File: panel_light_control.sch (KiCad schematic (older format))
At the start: 70 parts, among them J1 Conn_01x02, J6 Conn_01x04, Q1 IRF540N, Q2 IRF540N, Q3 IRF540N, U1 L7805, U2 LM324

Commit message: RGB current sink placed and routed. All placement should be done now, next: check barrel jack footprint, do power routing, think about input protection for GPIOs, possibly add resistor arrays, route GP signals.
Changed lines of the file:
@@
 	8950 1850 9150 1850
-Wire Wire Line
-	7450 2150 7150 2150
-Connection ~ 7150 2150
-Wire Wire Line
-	7150 2150 7150 2300
-Wire Wire Line
-	6700 2150 6800 2150
-Wire Wire Line
-	6800 2300 6800 2150
-Connection ~ 6800 2150
-Wire Wire Line
-	6800 2150 7150 2150
 Wire Wire Line
 	6800 2600 6800 2700
@@
 	0    -1   1    0
 $EndComp
+Wire Wire Line
+	6800 2150 6700 2150
+Wire Wire Line
+	6800 2150 6800 2300
+Wire Wire Line
+	6800 2150 7150 2150
+Wire Wire Line
+	7150 2150 7150 2300
+Connection ~ 6800 2150
+Wire Wire Line
+	7150 2150 7450 2150
+Connection ~ 7150 2150
 $EndSCHEMATC

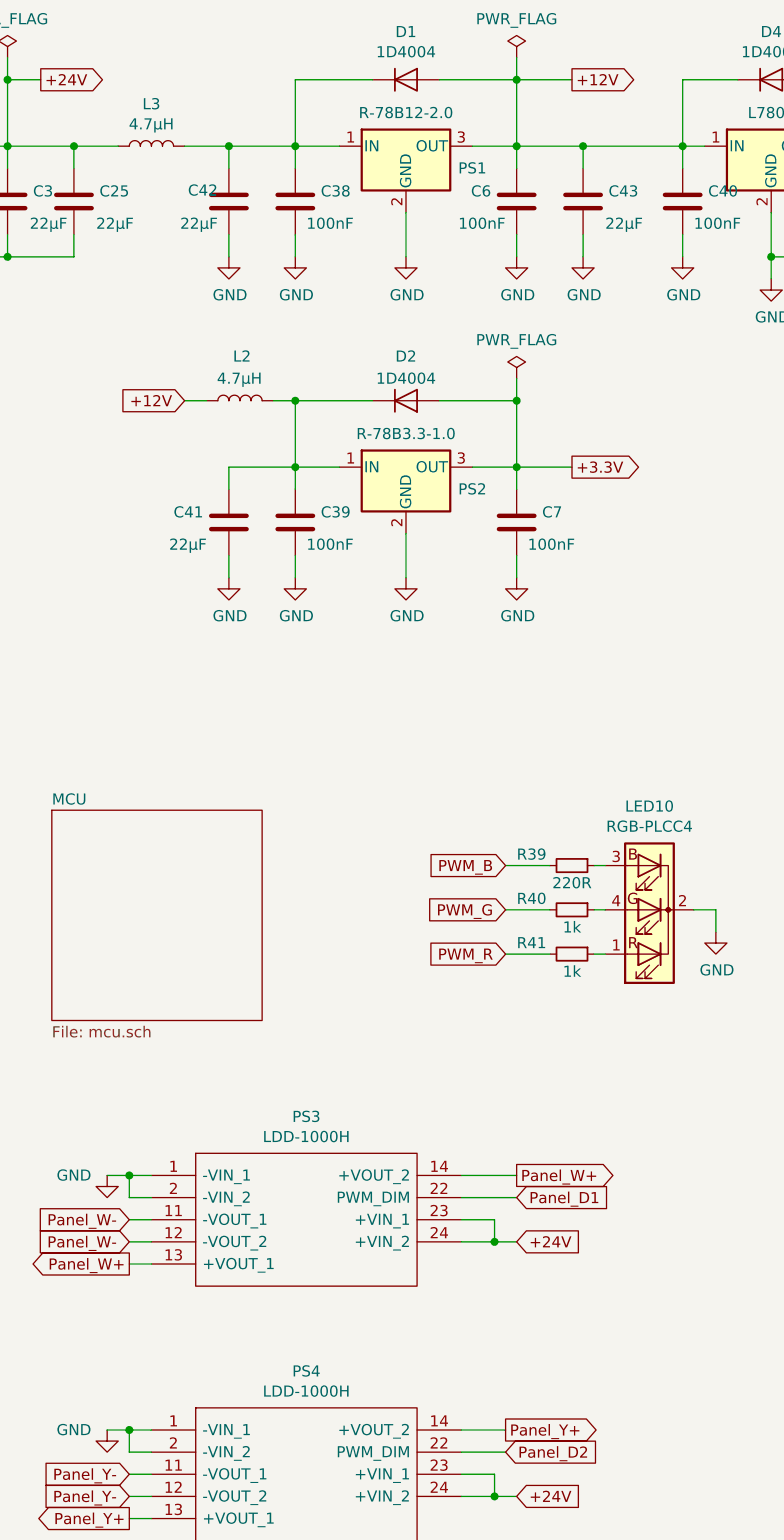
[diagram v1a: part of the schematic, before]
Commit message: PS1-> Panel1, PS2-> Panel2, PS12->12V, PS33-> 3.3V.
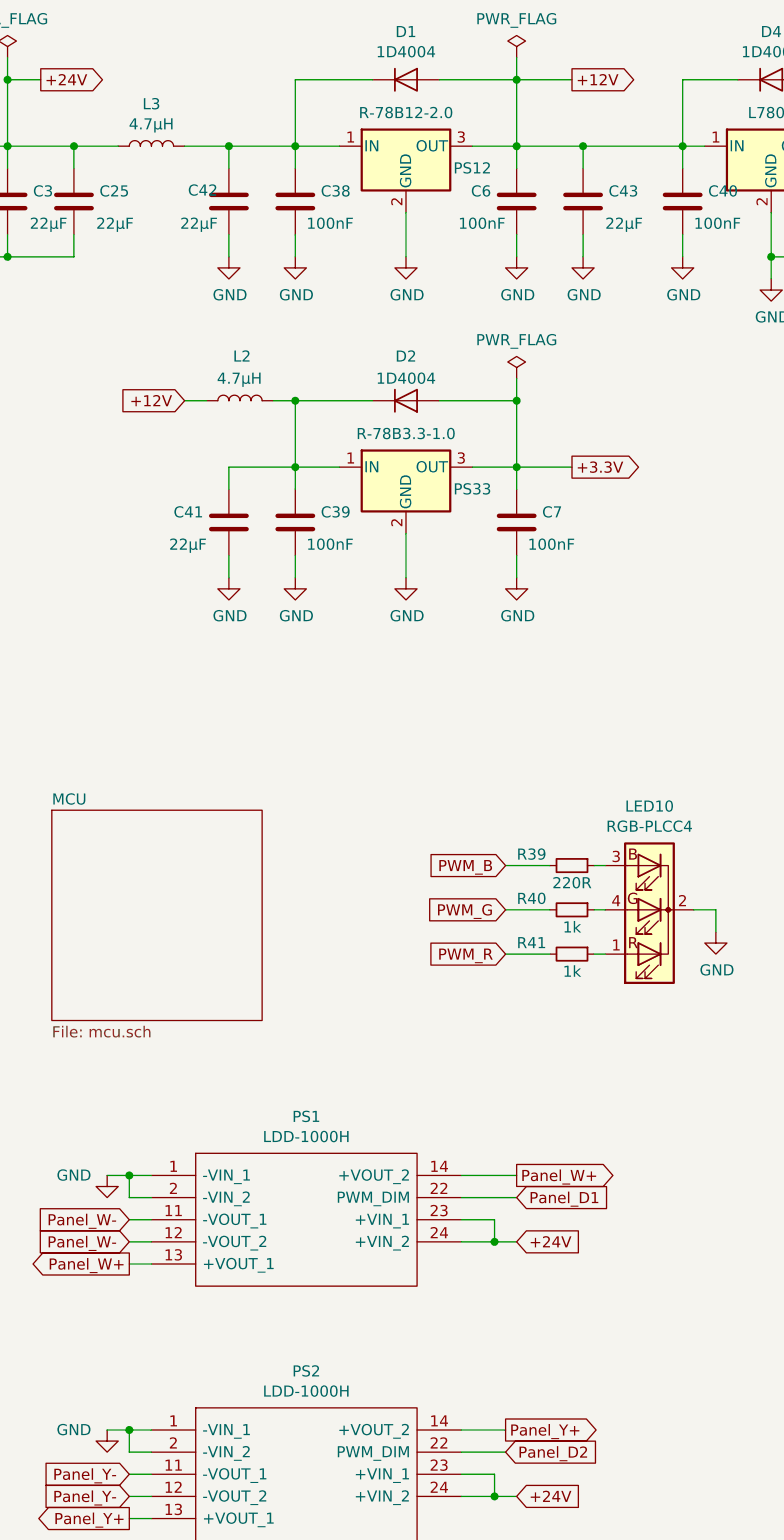
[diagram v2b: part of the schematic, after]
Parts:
- renumbered PS3 to PS1, PS1 to PS12, PS4 to PS2, PS2 to PS33
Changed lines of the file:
@@
 Connection ~ 2000 1200
 $Comp
-L panel_light_control-rescue:LDD-1000H-SamacSys_Parts PS4
+L panel_light_control-rescue:LDD-1000H-SamacSys_Parts PS2
 U 1 1 5BB7E2A0
 P 2650 7000
-F 0 "PS4" H 3350 7265 50  0000 C CNN
+F 0 "PS2" H 3350 7265 50  0000 C CNN
 F 1 "LDD-1000H" H 3350 7174 50  0000 C CNN
 F 2 "SamacSys_Parts:LDD-700H" H 3900 7100 50  0001 L CNN
@@
 $EndComp
 $Comp
-L panel_light_control-rescue:LDD-1000H-SamacSys_Parts PS3
+L panel_light_control-rescue:LDD-1000H-SamacSys_Parts PS1
 U 1 1 5BB8F859
 P 2650 5850
-F 0 "PS3" H 3350 6115 50  0000 C CNN
+F 0 "PS1" H 3350 6115 50  0000 C CNN
 F 1 "LDD-1000H" H 3350 6024 50  0000 C CNN
 F 2 "SamacSys_Parts:LDD-700H" H 3900 5950 50  0001 L CNN
@@
 $EndComp
 $Comp
-L Regulator_Switching:R-78B12-2.0 PS1
+L Regulator_Switching:R-78B12-2.0 PS12
 U 1 1 5BB902DF
 P 3800 1200
-F 0 "PS1" H 4100 1100 50  0000 C CNN
+F 0 "PS12" H 4100 1100 50  0000 C CNN
 F 1 "R-78B12-2.0" H 3800 1350 50  0000 C CNN
 F 2 "Converter_DCDC:Converter_DCDC_RECOM_R-78B-2.0_THT" H 4750 1300 50  0001 L CNN
@@
 $EndComp
 $Comp
-L Regulator_Switching:R-78B3.3-2.0 PS2
+L Regulator_Switching:R-78B3.3-2.0 PS33
 U 1 1 5BB90449
 P 3800 2650
-F 0 "PS2" H 4100 2550 50  0000 C CNN
+F 0 "PS33" H 4100 2550 50  0000 C CNN
 F 1 "R-78B3.3-1.0" H 3800 2800 50  0000 C CNN
 F 2 "Converter_DCDC:Converter_DCDC_RECOM_R-78B-2.0_THT" H 4850 2750 50  0001 L CNN

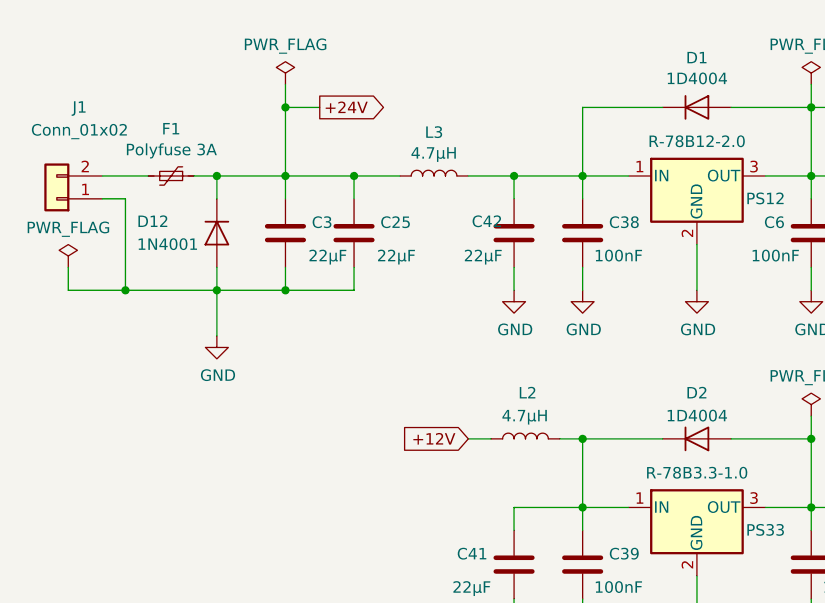
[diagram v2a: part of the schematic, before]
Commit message: add CAN termination jumper, switch-mode DCDC power routing and current sink routing done. Barrel jacks still need swapping?
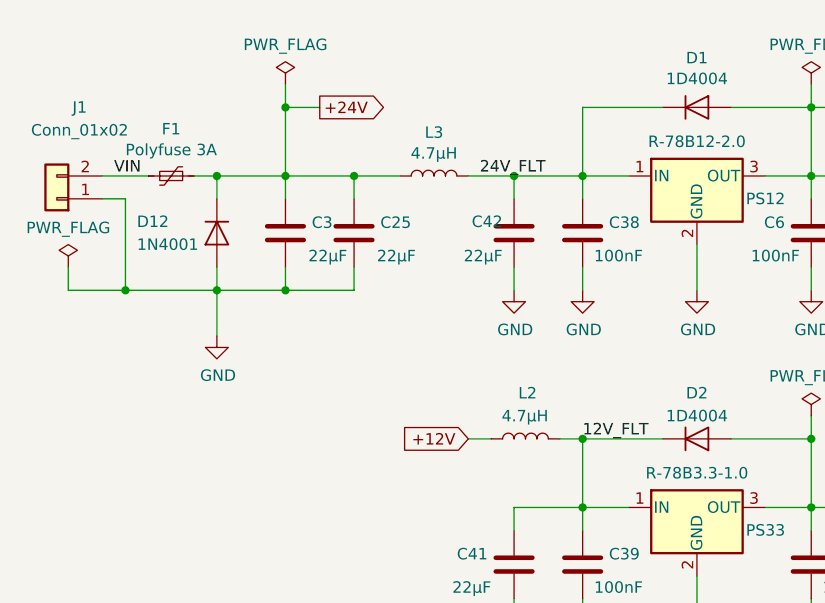
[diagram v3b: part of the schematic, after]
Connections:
- net VIN: now reaches F1.2, J1.2 (Pin_2)
- net 24V_FLT: now reaches C38.1, C42.1, D1.1 (K), L3.2, PS12.1 (IN)
- net 12V_FLT: now reaches C39.1, C41.1, D2.1 (K), L2.2, PS33.1 (IN)
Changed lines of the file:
@@
 	7150 2150 7450 2150
 Connection ~ 7150 2150
+Text Label 1250 1200 0    50   ~ 0
+VIN
+Text Label 2850 1200 0    50   ~ 0
+24V_FLT
+Text Label 3300 2350 0    50   ~ 0
+12V_FLT
 $EndSCHEMATC

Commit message: change I2S connector footprint back from 11 pin to 10 pin (MCK, SCK, WS... missing something?). More silkscreen clean-up and a bit of routing.
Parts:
- JTAG1: value Conn_01x06 -> Conn_01x07; footprint Connector_JST:JST_PH_S6B-PH-K_1x06_P2.00mm_Horizontal -> Connector_JST:JST_PH_S7B-PH-K_1x07_P2.00mm_Horizontal; symbol Connector_Generic:Conn_01x06 -> Connector_Generic:Conn_01x07
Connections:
- net +3.3V: now also JTAG1.7 (Pin_7)
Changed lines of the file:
@@
 	10400 5300 10200 5300
 $Comp
-L Connector_Generic:Conn_01x06 JTAG1
+L Connector_Generic:Conn_01x07 JTAG1
 U 1 1 5C66DBBA
-P 10600 2100
-F 0 "JTAG1" H 10680 2092 50  0000 L CNN
-F 1 "Conn_01x06" H 10680 2001 50  0000 L CNN
-F 2 "Connector_JST:JST_PH_S6B-PH-K_1x06_P2.00mm_Horizontal" H 10600 2100 50  0001 C CNN
-F 3 "~" H 10600 2100 50  0001 C CNN
-	1    10600 2100
-	1    0    0    -1
-$EndComp
-Text GLabel 10200 1900 0    50   Input ~ 0
+P 10600 2050
+F 0 "JTAG1" H 10680 2042 50  0000 L CNN
+F 1 "Conn_01x07" H 10680 1951 50  0000 L CNN
+F 2 "Connector_JST:JST_PH_S7B-PH-K_1x07_P2.00mm_Horizontal" H 10600 2050 50  0001 C CNN
+F 3 "~" H 10600 2050 50  0001 C CNN
+	1    10600 2050
+	1    0    0    -1
+$EndComp
+Text GLabel 10200 1750 0    50   Input ~ 0
 JTMS
-Text GLabel 10200 2000 0    50   Input ~ 0
+Text GLabel 10200 1850 0    50   Input ~ 0
 JTCK
-Text GLabel 10200 2100 0    50   Input ~ 0
+Text GLabel 10200 1950 0    50   Input ~ 0
 JTDI
-Text GLabel 10200 2200 0    50   Input ~ 0
+Text GLabel 10200 2050 0    50   Input ~ 0
 JTDO
-Text GLabel 10200 2300 0    50   Input ~ 0
+Text GLabel 10200 2150 0    50   Input ~ 0
 JTRST
 Wire Wire Line
-	10400 1900 10200 1900
-Wire Wire Line
-	10200 2000 10400 2000
-Wire Wire Line
-	10400 2100 10200 2100
-Wire Wire Line
-	10200 2200 10400 2200
-Wire Wire Line
-	10400 2300 10200 2300
+	10400 1750 10200 1750
+Wire Wire Line
+	10200 1850 10400 1850
+Wire Wire Line
+	10400 1950 10200 1950
+Wire Wire Line
+	10200 2050 10400 2050
+Wire Wire Line
+	10400 2150 10200 2150
 $Comp
 L power:GND #PWR04
 U 1 1 5C8842DC
-P 10300 2400
-F 0 "#PWR04" H 10300 2150 50  0001 C CNN
-F 1 "GND" H 10150 2350 50  0000 C CNN
-F 2 "" H 10300 2400 50  0001 C CNN
-F 3 "" H 10300 2400 50  0001 C CNN
-	1    10300 2400
-	1    0    0    -1
-$EndComp
-Wire Wire Line
-	10300 2400 10400 2400
+P 10300 2450
+F 0 "#PWR04" H 10300 2200 50  0001 C CNN
+F 1 "GND" H 10150 2400 50  0000 C CNN
+F 2 "" H 10300 2450 50  0001 C CNN
+F 3 "" H 10300 2450 50  0001 C CNN
+	1    10300 2450
+	1    0    0    -1
+$EndComp
+Wire Wire Line
+	10300 2250 10400 2250
 Text GLabel 10200 4800 0    50   Input ~ 0
 SPI0_CS0
@@
 Text Label 3300 2350 0    50   ~ 0
 12V_FLT
+Text GLabel 10200 2350 0    50   Input ~ 0
++3.3V
+Wire Wire Line
+	10200 2350 10400 2350
+Wire Wire Line
+	10300 2250 10300 2450
 $EndSCHEMATC

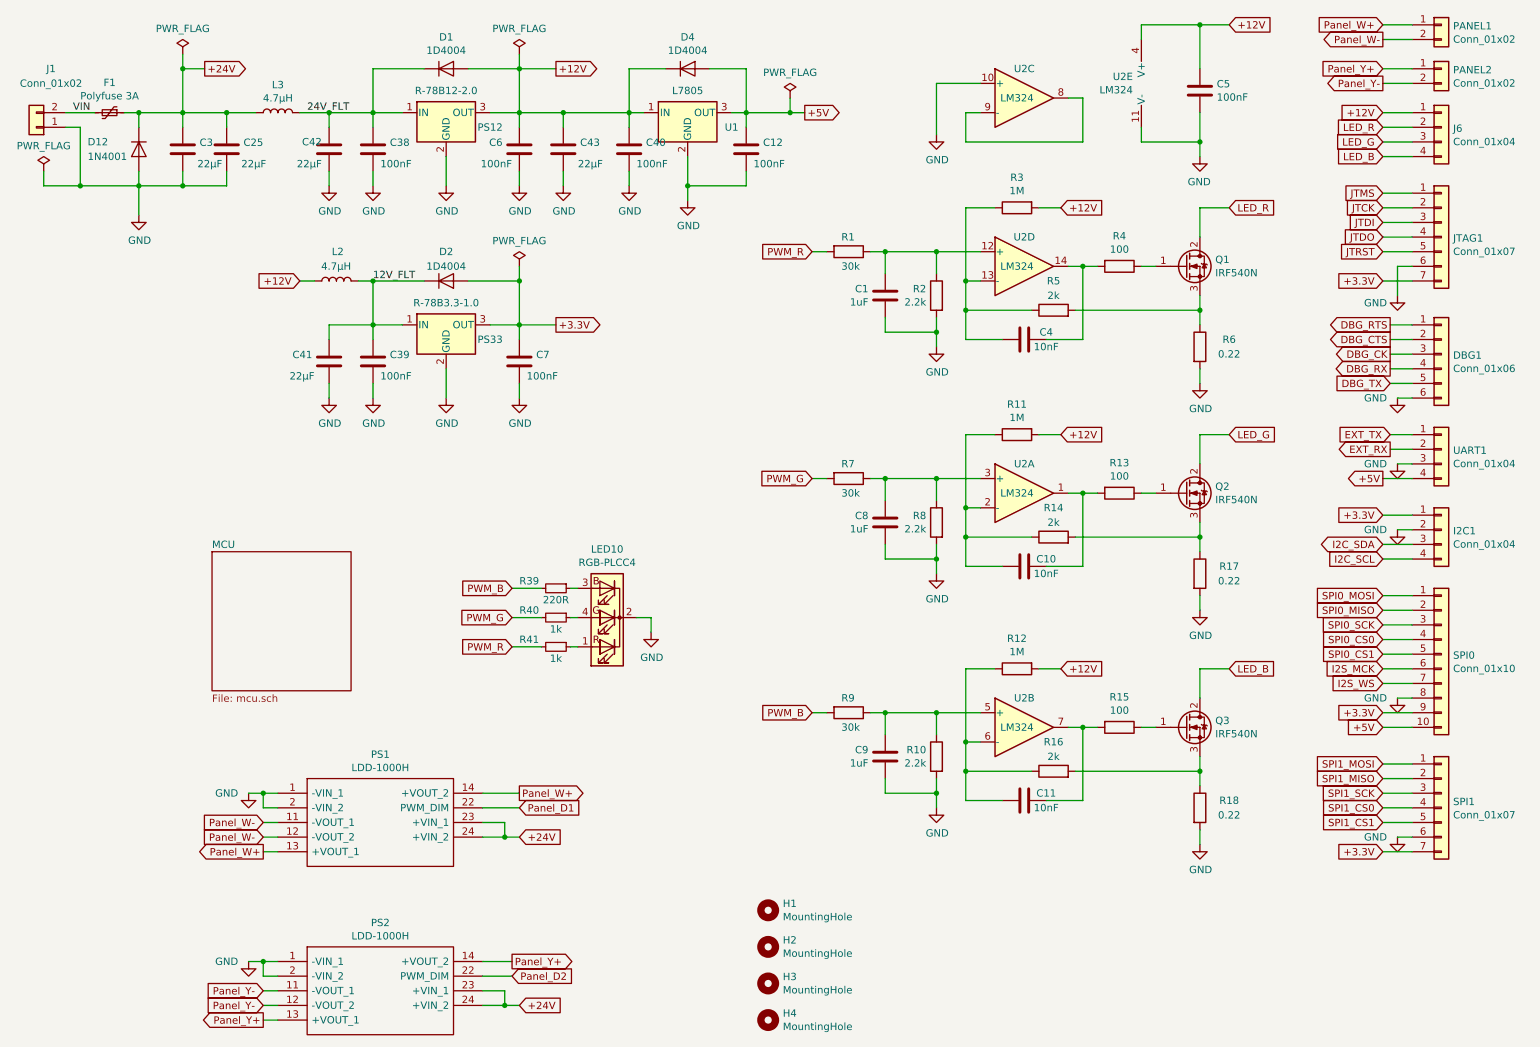
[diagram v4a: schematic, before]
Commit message: routing almost done. ToDo: fix symbols to include shielding on some connectors. finish routing. Add GND copper pour on bottom side.
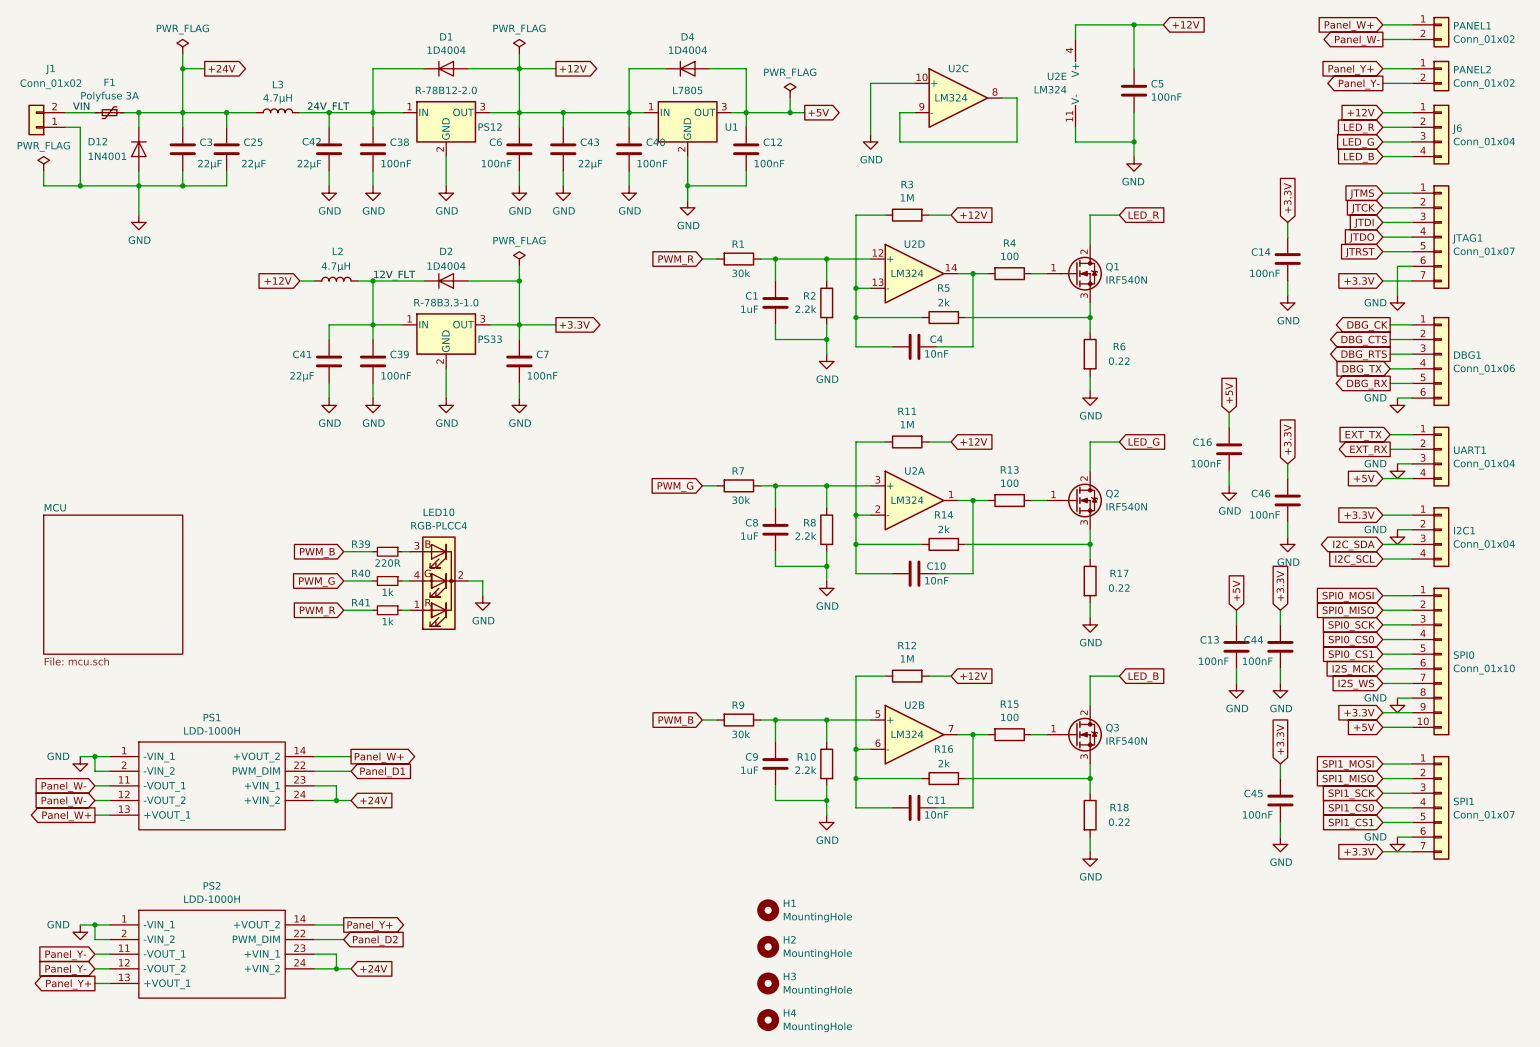
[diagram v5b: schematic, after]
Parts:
- added C13, C14, C16, C44, C45, C46: 100nF, Capacitor_SMD:C_0603_1608Metric, symbol Device:C
- SPI0: footprint Connector_JST:JST_PH_S11B-PH-K_1x11_P2.00mm_Horizontal -> Connector_JST:JST_PH_S10B-PH-K_1x10_P2.00mm_Horizontal
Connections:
- net +3.3V: now also C14.1, C44.1, C45.1, C46.1
- net +5V: now also C13.1, C16.1
- net DBG_CK: now also DBG1.1 (Pin_1); no longer DBG1.3 (Pin_3)
- net DBG_RTS: now also DBG1.3 (Pin_3); no longer DBG1.1 (Pin_1)
- net DBG_RX: now also DBG1.5 (Pin_5); no longer DBG1.4 (Pin_4)
- net DBG_TX: now also DBG1.4 (Pin_4); no longer DBG1.5 (Pin_5)
- net GND: now also C13.2, C14.2, C16.2, C44.2, C45.2, C46.2
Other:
- moved on the sheet: C1, C10, C11, C4, C5, C8, C9, LED10, PS1, PS2, Q1, Q2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

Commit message: all connector shields are now connected to ground. Note HR911105A LED pins are offset by 4.9mm whereas the WE LED pins are at 4.1mm. Can still fit the WE part? but it won't be pretty.
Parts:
- PANEL1, PANEL2: symbol Connector_Generic:Conn_01x02 -> Connector_Generic_MountingPin:Conn_01x02_MountingPin
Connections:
- net GND: now also PANEL1.MP (MountPin), PANEL2.MP (MountPin)
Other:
- moved on the sheet: DBG1, I2C1, J6, JTAG1, SPI0, SPI1, UART1

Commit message: lots of labels!
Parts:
- added C?: 4.7uF, Capacitor_SMD:C_0805_2012Metric, symbol Device:C_Small
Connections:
- net +5V: now also C?.1
- net GND: now also C?.2
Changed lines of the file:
@@
 Wire Wire Line
 	10700 1300 10600 1300
+$Comp
+L Device:C_Small C?
+U 1 1 5BF468BF
+P 6150 1450
+AR Path="/5BBC4BB7/5BF468BF" Ref="C?"  Part="1"
+AR Path="/5C1EFDBE/5BF468BF" Ref="C?"  Part="1"
+AR Path="/5C211DD3/5BF468BF" Ref="C?"  Part="1"
+AR Path="/5C211FC6/5BF468BF" Ref="C?"  Part="1"
+F 0 "C?" H 6050 1500 50  0000 R CNN
+F 1 "4.7uF" H 6050 1350 50  0000 R CNN
+F 2 "Capacitor_SMD:C_0805_2012Metric" H 6150 1450 50  0001 C CNN
+F 3 "~" H 6150 1450 50  0001 C CNN
+	1    6150 1450
+	-1   0    0    -1
+$EndComp
+Wire Wire Line
+	6150 1200 6150 1350
+Wire Wire Line
+	6150 1700 5850 1700
+Wire Wire Line
+	6150 1550 6150 1700
+Connection ~ 5850 1700
 $EndSCHEMATC
